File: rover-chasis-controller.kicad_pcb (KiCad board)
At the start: 2 copper layers, 100 x 100 mm, 141 parts, among them J10 GPS Interface, J11 Compass Connection (I2C), J15 External LED (Red), J16 External LED (Yellow), J17 External LED (Green), J22 Ultrasonic Sensor Inputs, J26 Screw_Terminal_01x02, J3 HR911105A_C12074, J36 Motor control, J37 Motor control, J38 Motor control, J39 Motor control, J40 Encoder, J41 Encoder, J42 Encoder, J43 Encoder, J7 TTL, J8 Ultrasonic Sensor Inputs, Q1 MMBT3904_C181119, Q11 MMBT3904_C181119, Q13 MMBT3904_C181119, Q14 MMBT3904_C181119, Q15 SUD50P10-43L-TP, Q17 MMBT3904_C181119, Q22 MMBT3904_C181119, Q23 MMBT3904_C181119, Q24 MMBT3904_C181119, Q25 MMBT3904_C181119, Q26 MMBT3904_C181119, Q27 MMBT3904_C181119, Q28 MMBT3904_C181119, Q29 MMBT3904_C181119, Q30 MMBT3904_C181119, Q31 MMBT3904_C181119, Q32 MMBT3904_C181119, Q33 MMBT3904_C181119, Q34 MMBT3904_C181119, Q35 MMBT3904_C181119, Q6 MMBT3904_C181119, U1 APT2012LVBC/D, U2 APT2012LVBC/D, U3 APT2012LVBC/D, U4 KSZ8081RNAIA-TR, U5 MPU-6050_C24112, U6 AP64500SP-13, U7 APT2012LVBC/D, X1 X1G004451000400

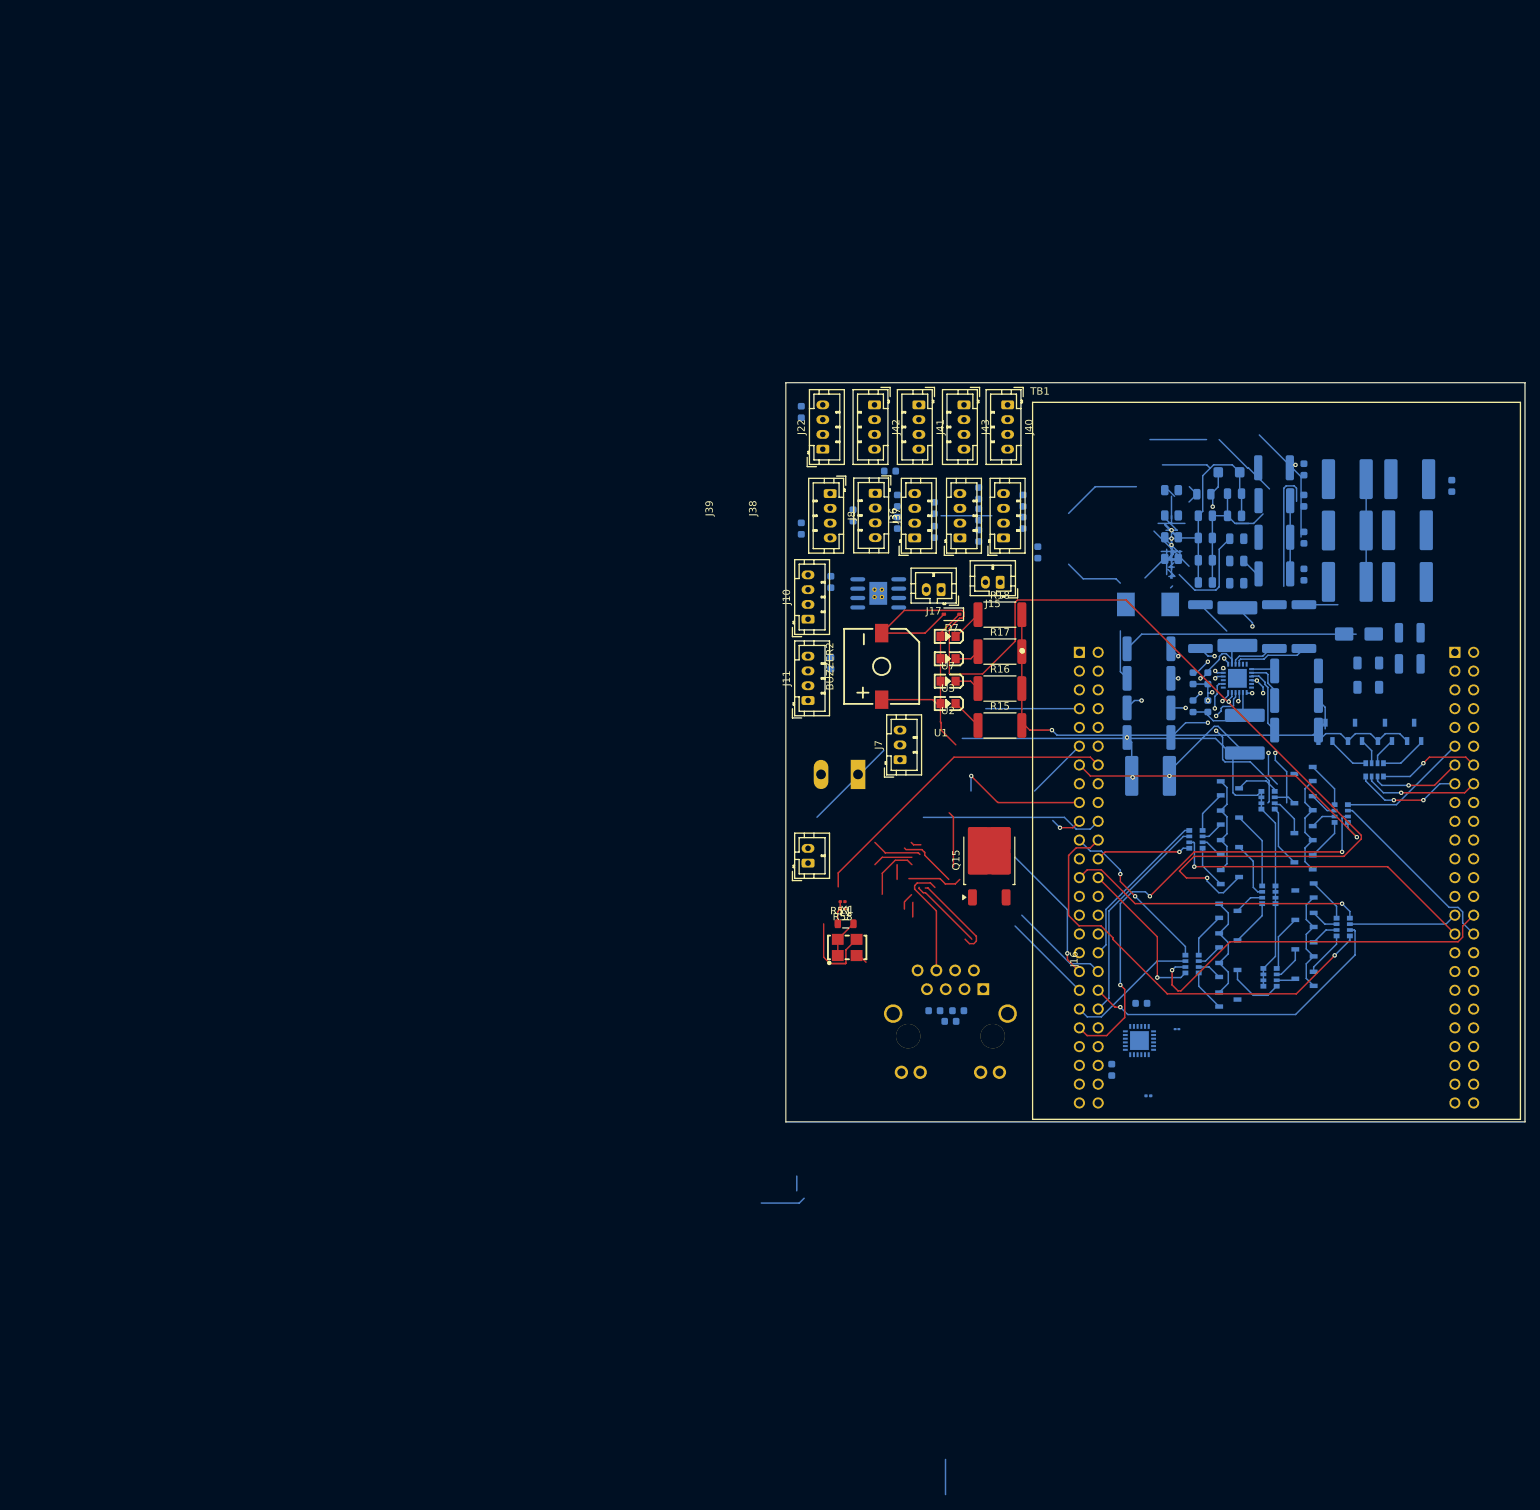
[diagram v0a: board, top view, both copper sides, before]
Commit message: Issue #1: Revised possible PCB design
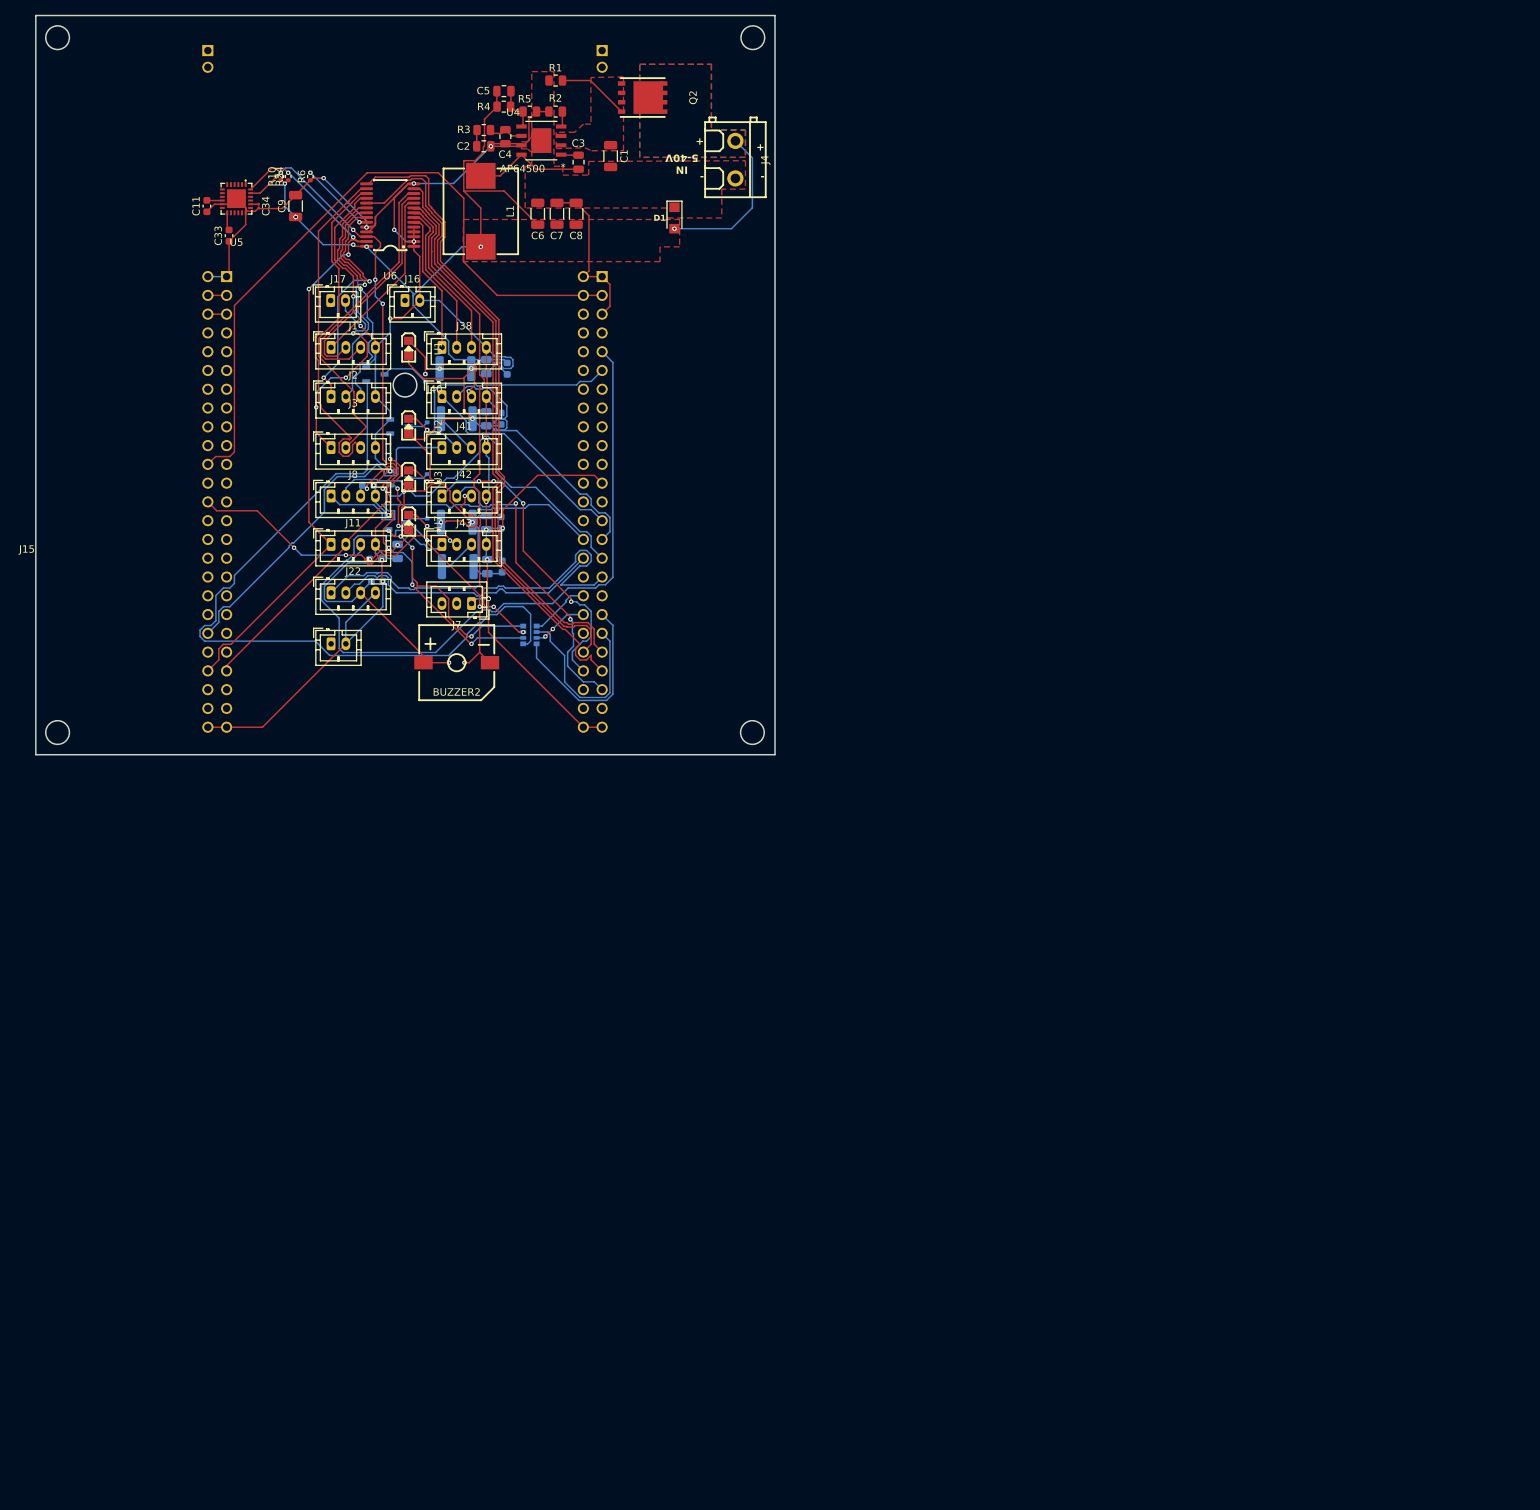
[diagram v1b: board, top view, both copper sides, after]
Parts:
- removed C17, C71, C72, C83, C84, C85, C86, C87, C88, C89, C90, C91, C92, C93, C94: 0.1uF, Capacitor_SMD:C_0603_1608Metric
- removed C18: 10uF, Capacitor_SMD:C_0805_2012Metric
- removed C53: 10uF, Capacitor_SMD:C_2220_5750Metric
- removed C54: 100nF, Capacitor_SMD:C_0805_2012Metric
- removed C55: 2.7nF, Capacitor_SMD:C_0805_2012Metric
- removed C56: 39pF, Capacitor_SMD:C_0805_2012Metric
- removed C57: 47pF, Capacitor_SMD:C_0805_2012Metric
- removed C58, C59, C60: 22 uF, Capacitor_SMD:C_2220_5750Metric
- removed C62: 0.1uF 200V, Capacitor_SMD:C_0603_1608Metric
- removed D10: SMF5V0A, Diode_SMD:D_SMF
- removed D11: SMAJ5.0A, Diode_SMD:D_SMA
- removed FB1: FerriteBead, Inductor_SMD:L_0603_1608Metric
- removed J10: GPS Interface, Connector_JST:JST_PH_B4B-PH-K_1x04_P2.00mm_Vertical
- removed J26: Screw_Terminal_01x02, TerminalBlock:TerminalBlock_Altech_AK300-2_P5.00mm
- removed J36, J37, J39: Motor control, Connector_JST:JST_PH_B4B-PH-K_1x04_P2.00mm_Vertical
- removed L4: 4.7uH, easyeda2kicad:IND-SMD_L7.0-W6.6
- removed Q1, Q11, Q13, Q17, Q22, Q23, Q24, Q25, Q26, Q27, Q28, Q29, Q30, Q31, Q32, Q6: MMBT3904_C181119, easyeda2kicad:SOT-23-3_L2.9-W1.6-P1.90-LS2.8-BR
- removed Q15: SUD50P10-43L-TP, Package_TO_SOT_SMD:TO-252-2
- removed R16, R17, R18: 220, Resistor_SMD:R_2512_6332Metric
- removed R25: 4.3k, Resistor_SMD:R_1210_3225Metric
- removed R57, R58: 330, Resistor_SMD:R_0201_0603Metric
- removed R59, R60, R61, R62, R63, R71, R72, R73, R74: 24, Resistor_SMD:R_2512_6332Metric
- removed R75: 47k, Resistor_SMD:R_0201_0603Metric
- removed R76: 10k, Resistor_SMD:R_1206_3216Metric
- removed R77: 47k T+-1%, Resistor_SMD:R_1206_3216Metric
- removed R78: 200k, Resistor_SMD:R_0805_2012Metric
- removed R79: 16k, Resistor_SMD:R_0805_2012Metric
- removed R80: 120k, Resistor_SMD:R_0805_2012Metric
- removed R81: 22.1k, Resistor_SMD:R_0805_2012Metric
- removed RN10, RN11, RN12: 4D03WGJ0102T5E (10k), easyeda2kicad:RES-ARRAY-SMD_0603-8P-L3.2-W1.6-BL
- removed RN2, RN3, RN4, RN5: 4D03WGJ0102T5E (1k), easyeda2kicad:RES-ARRAY-SMD_0603-8P-L3.2-W1.6-BL
- removed X1: X1G004451000400, easyeda2kicad:OSC-SMD_4P-L5.0-W3.2-BL_SG5032
- added D1: SMF5V0A, Diode_SMD:D_SMF, F.Cu at (86.5, 27.4)
- added J1: Motor control, Connector_JST:JST_PH_B4B-PH-K_1x04_P2.00mm_Vertical, F.Cu at (40.0, 44.9)
- added J2: Motor control, Connector_JST:JST_PH_B4B-PH-K_1x04_P2.00mm_Vertical, F.Cu at (40.0, 51.5)
- added J4: Screw_Terminal_01x02, easyeda2kicad:CONN-TH_2P-P5.08, F.Cu at (94.7, 19.5)
- added Q2: HSBA100P04_C2987717, easyeda2kicad:DFN-8_L5.7-W5.1-P1.27-LS6.1-BL-1, F.Cu at (82.2, 11.1)
- added R10: 4.3k, Resistor_SMD:R_0402_1005Metric, F.Cu at (33.2, 21.8)
- added R2: 200k, Resistor_SMD:R_0805_2012Metric, F.Cu at (70.4, 13.0)
- added R3: 16k, Resistor_SMD:R_0805_2012Metric, F.Cu at (60.7, 15.5)
- added R4: 120k, Resistor_SMD:R_0805_2012Metric, F.Cu at (63.4, 12.3)
- added R5: 22.1k, Resistor_SMD:R_0805_2012Metric, F.Cu at (66.9, 13.0)
- added R6: 10k, Resistor_SMD:R_0402_1005Metric, F.Cu at (37.2, 21.8)
- added R7: 220, Resistor_SMD:R_0402_1005Metric, B.Cu at (53.0, 55.5)
- added R8: 220, Resistor_SMD:R_0402_1005Metric, B.Cu at (53.0, 62.5)
- added R9: 220, Resistor_SMD:R_0402_1005Metric, B.Cu at (53.0, 68.6)
- C1: value 0.1uF -> 10uF; footprint Capacitor_SMD:C_0603_1608Metric -> Capacitor_SMD:C_1206_3216Metric; moved to F.Cu
- C11, C33, C34, U5: moved to F.Cu
- C2: value 22uF -> 2.7nF; footprint Capacitor_SMD:C_2220_5750Metric -> Capacitor_SMD:C_0805_2012Metric; moved to F.Cu
- C3: value 2.2uF -> 100nF; footprint Capacitor_SMD:C_2220_5750Metric -> Capacitor_SMD:C_0805_2012Metric; moved to F.Cu
- C4: value 0.1uF -> 39pF; footprint Capacitor_SMD:C_0603_1608Metric -> Capacitor_SMD:C_0805_2012Metric; moved to F.Cu
- C5: value 22pF -> 47pF; footprint Capacitor_SMD:C_2220_5750Metric -> Capacitor_SMD:C_0805_2012Metric; moved to F.Cu
- C6, C8: value 0.1uF -> 22 uF; footprint Capacitor_SMD:C_0603_1608Metric -> Capacitor_SMD:C_1206_3216Metric; moved to F.Cu
- C7: value 22uF -> 22 uF; footprint Capacitor_SMD:C_2220_5750Metric -> Capacitor_SMD:C_1206_3216Metric; moved to F.Cu
- C9: value 22uF -> 10uF; footprint Capacitor_SMD:C_2220_5750Metric -> Capacitor_SMD:C_1206_3216Metric; moved to F.Cu
- D7: moved to B.Cu
- J3: value HR911105A_C12074 -> Motor control; footprint easyeda2kicad:RJ45-TH_HR911105A -> Connector_JST:JST_PH_B4B-PH-K_1x04_P2.00mm_Vertical; moved to F.Cu
- L1: value BLM21PG331SN1D -> 3.3uH; footprint Inductor_SMD:L_0805_2012Metric -> easyeda2kicad:IND-SMD_L11.6-W10.1
- R1: value 24 -> 47k; footprint Resistor_SMD:R_2512_6332Metric -> Resistor_SMD:R_0805_2012Metric; moved to F.Cu
- R15: footprint Resistor_SMD:R_2512_6332Metric -> Resistor_SMD:R_0402_1005Metric; moved to B.Cu
- R24: footprint Resistor_SMD:R_1210_3225Metric -> Resistor_SMD:R_0402_1005Metric; moved to F.Cu
- TB1: footprint STM32F4DISCOVERY:MODULE_STM32F4DISCOVERY -> stm32:MODULE_STM32F4DISCOVERY; moved to B.Cu
- U4: value KSZ8081RNAIA-TR -> AP64500; footprint easyeda2kicad:QFN-24_L4.0-W4.0-P0.50-BL-EP2.6 -> easyeda2kicad:AP64500SP-13; moved to F.Cu
- U6: value AP64500SP-13 -> PCA9685PW,118; footprint easyeda2kicad:SOIC-8_L4.9-W3.9-P1.27-LS6.0-BL-EP-1 -> easyeda2kicad:TSSOP-28_L9.7-W4.4-P0.65-LS6.4-TL; moved to F.Cu
- moved C11 169.2 mm to (23.2, 25.8)
- moved U5 167.0 mm to (27.2, 24.8)
- moved C34 166.8 mm to (30.2, 25.8), turned to -90 degrees
- moved R24 163.8 mm to (34.2, 21.8), turned to 90 degrees
- moved C33 161.3 mm to (26.2, 29.8), turned to 90 degrees
- moved Q35 140.4 mm to (49.0, 68.5), turned to 180 degrees
- moved C9 139.5 mm to (35.2, 25.8)
- moved Q34 137.7 mm to (49.2, 62.6), turned to 180 degrees
- moved Q14 137.3 mm to (46.0, 48.5), turned to 180 degrees
- moved Q33 135.7 mm to (49.2, 55.6), turned to 180 degrees
- moved C2 130.1 mm to (60.7, 17.7), turned to 0 degrees
- moved C6 129.0 mm to (68.0, 26.8), turned to 90 degrees
- moved TB1 128.4 mm to (50.0, 50.0), turned to 180 degrees
- moved C5 127.4 mm to (63.4, 10.2), turned to 0 degrees
- moved C3 125.7 mm to (73.5, 19.8), turned to -90 degrees
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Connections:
- BUZZER2 pad 2: /Buzzer_Collector -> /BUZZER_OUT
- C1 pad 1: GND -> unconnected-(C1-Pad1)
- C1 pad 2: Net-(U4-VDD_1.2) -> GND
- C2 pad 1: Net-(U4-VDDA_3.3) -> Net-(C2-Pad1)
- C3 pad 1: Net-(U4-VDD_1.2) -> Net-(U4-BST)
- C3 pad 2: GND -> Net-(U4-SW)
- C4 pad 1: GND -> Net-(U4-COMP)
- C4 pad 2: Net-(U4-VDDA_3.3) -> GND
- C5 pad 1: GND -> VCC (5V)
- C5 pad 2: Net-(X1-OUT) -> Net-(U4-FB)
- C6 pad 1: GND -> VCC (5V)
- C6 pad 2: Net-(X1-OE/~{ST}) -> GND
- C7 pad 1: Net-(X1-OE/~{ST}) -> VCC (5V)
- C8 pad 1: GND -> VCC (5V)
- C8 pad 2: VCC (3.3V) -> GND
- C9 pad 1: VCC (3.3V) -> VCC (5V)
- D7 pad 2: /Buzzer_Collector -> /BUZZER_OUT
- J11 pad 1: /COMPASS_SDA -> /SDA
- J11 pad 2: /COMPASS_SCL -> /SCL
- J3 pad 1: /TXP -> /MOTOR4_PWM
- J3 pad 2: /TXM -> /MOTOR4_FWD
- J3 pad 3: /RXP -> /MOTOR4_RVR
- J3 pad 4: Net-(C72-Pad1) -> GND
- J38 pad 1: /Motor_PWM_Collector_4 -> /MOTOR1_PWM
- J38 pad 2: /Motor_F_Collector_4 -> /MOTOR1_FWD
- J38 pad 3: /Motor_R_Collector_4 -> /MOTOR1_RVR
- J7 pad 1: /TTL_RX -> GND
- J7 pad 3: GND -> /TTL_RX
- L1 pad 1: VCC (3.3V) -> Net-(U4-SW)
- L1 pad 2: Net-(X1-OE/~{ST}) -> VCC (5V)
- R1 pad 1: Net-(U4-XI) -> Net-(Q2-G)
- R1 pad 2: Net-(X1-OUT) -> GND
- R24 pad 1: VCC (3V) -> VCC (5V)
- R24 pad 2: /COMPASS_SDA -> /SDA
- TB1 pad P1_11: /ETH_REF_CLK -> /ENC2_B
- TB1 pad P1_12: /TTL_TX -> unconnected-(TB1-PA0-WKUP-PadP1_12)
- TB1 pad P1_13: /MOTOR2_PWM -> unconnected-(TB1-PA3-PadP1_13)
- TB1 pad P1_14: /ETH_MDIO -> unconnected-(TB1-PA2-PadP1_14)
- TB1 pad P1_15: /ENC2_A -> unconnected-(TB1-PA5-PadP1_15)
- TB1 pad P1_16: /POWER_SUPPLY_ADC -> unconnected-(TB1-PA4-PadP1_16)
- TB1 pad P1_17: /ETH_CRS_DV -> unconnected-(TB1-PA7-PadP1_17)
- TB1 pad P1_18: /ENC3_A -> unconnected-(TB1-PA6-PadP1_18)
- TB1 pad P1_19: /ETH_RXD1 -> unconnected-(TB1-PC5-PadP1_19)
- TB1 pad P1_20: /ETH_RXD0 -> unconnected-(TB1-PC4-PadP1_20)
- TB1 pad P1_21: /MOTOR4_PWM -> unconnected-(TB1-PB1-PadP1_21)
- TB1 pad P1_22: /MOTOR3_PWM -> unconnected-(TB1-PB0-PadP1_22)
- TB1 pad P1_24: /BUZZER_OUT -> unconnected-(TB1-PB2-PadP1_24)
- TB1 pad P1_25: /LED_YELLOW -> unconnected-(TB1-PE7-PadP1_25)
- TB1 pad P1_26: /LED_GREEN -> unconnected-(TB1-PE8-PadP1_26)
- TB1 pad P1_30: unconnected-(TB1-PE12-PadP1_30) -> /US_SENSOR1_TRIG
- TB1 pad P1_33: unconnected-(TB1-PE15-PadP1_33) -> /US_SENSOR2_TRIG
- TB1 pad P1_34: /MOTOR1_PWM -> unconnected-(TB1-PB10-PadP1_34)
- TB1 pad P1_35: /ETH_TX_EN -> unconnected-(TB1-PB11-PadP1_35)
- TB1 pad P1_36: /ETH_TXD0 -> /LED_BLUE_4
- TB1 pad P1_37: /ETH_TXD1 -> /LED_BLUE_1
- TB1 pad P1_38: /MOTOR3_FWD -> /LED_BLUE_2
- TB1 pad P1_39: /MOTOR4_FWD -> /LED_BLUE_3
- TB1 pad P1_40: /MOTOR1_FWD -> unconnected-(TB1-PD8-PadP1_40)
- TB1 pad P1_41: /MOTOR2_FWD -> /LED_GREEN
- TB1 pad P1_42: /US_SENSOR1_TRIG -> /LED_YELLOW
- TB1 pad P1_43: /US_SENSOR2_TRIG -> /LED_RED
- TB1 pad P1_7: /ETH_MDC -> /POWER_SUPPLY_ADC
- TB1 pad P1_9: unconnected-(TB1-PC3-PadP1_9) -> /ENC3_A
- TB1 pad P2_11: /LED_RED -> unconnected-(TB1-PE6-PadP2_11)
- TB1 pad P2_13: /LED_BLUE_3 -> unconnected-(TB1-PE4-PadP2_13)
- TB1 pad P2_14: /LED_BLUE_4 -> unconnected-(TB1-PE5-PadP2_14)
- TB1 pad P2_15: /LED_BLUE_1 -> unconnected-(TB1-PE2-PadP2_15)
- TB1 pad P2_16: /LED_BLUE_2 -> unconnected-(TB1-PE3-PadP2_16)
- TB1 pad P2_23: /COMPASS_SCL -> unconnected-(TB1-PB6-PadP2_23)
- TB1 pad P2_24: /COMPASS_SDA -> unconnected-(TB1-PB7-PadP2_24)
- TB1 pad P2_26: unconnected-(TB1-PB5-PadP2_26) -> /ENC3_B
- TB1 pad P2_28: /ENC2_B -> unconnected-(TB1-PB3-PadP2_28)
- TB1 pad P2_29: /MOTOR3_RVR -> unconnected-(TB1-PD5-PadP2_29)
- TB1 pad P2_30: /MOTOR4_RVR -> unconnected-(TB1-PD6-PadP2_30)
- TB1 pad P2_31: /MOTOR1_RVR -> unconnected-(TB1-PD3-PadP2_31)
- TB1 pad P2_32: /MOTOR2_RVR -> unconnected-(TB1-PD4-PadP2_32)
- TB1 pad P2_34: /GPS_RX -> unconnected-(TB1-PD2-PadP2_34)
- TB1 pad P2_35: /GPS_TX -> unconnected-(TB1-PC12-PadP2_35)
- TB1 pad P2_38: /TTL_RX -> unconnected-(TB1-PC11-PadP2_38)
- TB1 pad P2_40: unconnected-(TB1-PA15-PadP2_40) -> /ENC2_A
- TB1 pad P2_43: /MPU_SCL -> /SCL
- TB1 pad P2_44: unconnected-(TB1-PA9-PadP2_44) -> /SDA
- TB1 pad P2_46: /MPU_SDA -> unconnected-(TB1-PC9-PadP2_46)
- TB1 pad P2_48: /ENC3_B -> unconnected-(TB1-PC7-PadP2_48)
- U4 pad 1: Net-(U4-VDD_1.2) -> Net-(U4-BST)
- U4 pad 2: Net-(U4-VDDA_3.3) -> unconnected-(C1-Pad1)
- U4 pad 3: /RXM -> unconnected-(C1-Pad1)
- U4 pad 4: /RXP -> Net-(U4-RT/CLK)
- U4 pad 5: /TXM -> Net-(U4-FB)
- U4 pad 6: /TXP -> Net-(U4-COMP)
- U4 pad 7: unconnected-(U4-XO-Pad7) -> GND
- U4 pad 8: Net-(U4-XI) -> Net-(U4-SW)
- U5 pad 23: /MPU_SCL -> /SCL
- U5 pad 24: /MPU_SDA -> /SDA
- U6 pad 1: Net-(U6-BST) -> GND
- U6 pad 2: Net-(Q15-S) -> GND
- U6 pad 3: Net-(Q15-S) -> GND
- U6 pad 4: Net-(U6-RT/CLK) -> GND
- U6 pad 5: Net-(U6-FB) -> GND
- U6 pad 6: Net-(U6-COMP) -> /MOTOR1_PWM
- U6 pad 7: GND -> /MOTOR1_FWD
- U6 pad 8: Net-(U6-SW) -> /MOTOR1_RVR
- U6 pad 9: GND -> /BUZZER_OUT
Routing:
- net GND: track 174.1 -> 349.1 mm, vias 6 -> 21
- net /Buzzer_Collector: track 144.8 -> 0.00 mm, vias 1 -> 0
- net /ENC3_A: track 0.00 -> 104.5 mm
- net /transistor_array4/B1: track 5.64 -> 101.1 mm
- net Net-(TB1-VDD-PadP1_3): track 0.00 -> 93.2 mm
- net /SDA: track 0.00 -> 93.0 mm, vias 0 -> 4
- net /SCL: track 0.00 -> 92.8 mm, vias 0 -> 4
- net VCC (5V): track 169.9 -> 252.6 mm, vias 1 -> 18
- net /LED_GREEN: track 20.9 -> 86.0 mm, vias 1 -> 0
- net /LED_RED: track 17.7 -> 79.9 mm
- net /BUZZER_OUT: track 12.9 -> 71.2 mm
- net /US_SENSOR2_TRIG: track 0.00 -> 53.5 mm
- net /US_SENSOR1_ECHO: track 0.00 -> 51.3 mm
- net /LED_Collector_1: track 57.3 -> 6.55 mm, vias 1 -> 0
- net /ENC2_A: track 0.00 -> 48.6 mm
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- added copper zone on F.Cu, net GND
- added copper zone on B.Cu, net VCC (5V)
- added copper zone on F.Cu, net VCC (5V)
- added copper zone on F.Cu, net unconnected-(C1-Pad1)
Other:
- outline, holes or cut-outs redrawn
- board text added: "+"
- board text added: "-"
- board text added: "IN 5-40V"

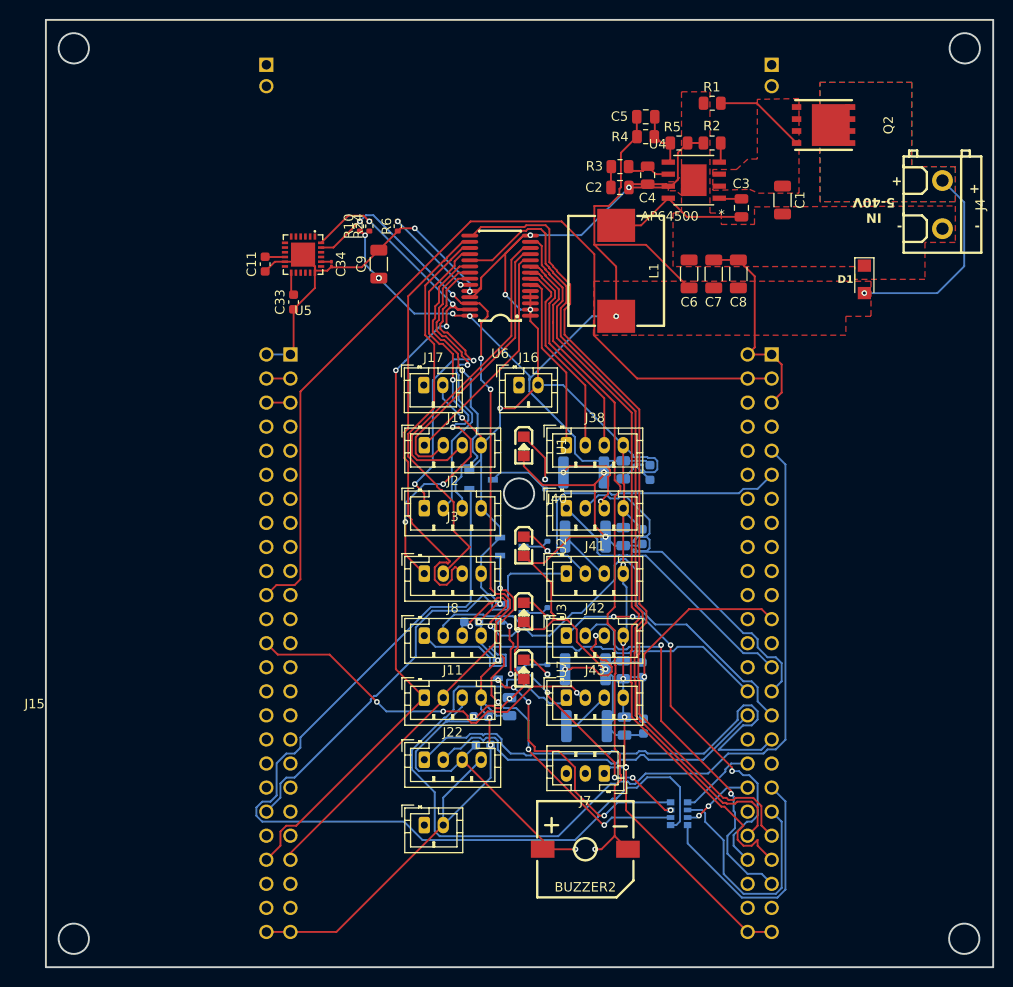
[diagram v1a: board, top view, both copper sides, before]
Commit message: Issue #1: Updated PCB layout — mounting holes, silk screen, and DRC fixes
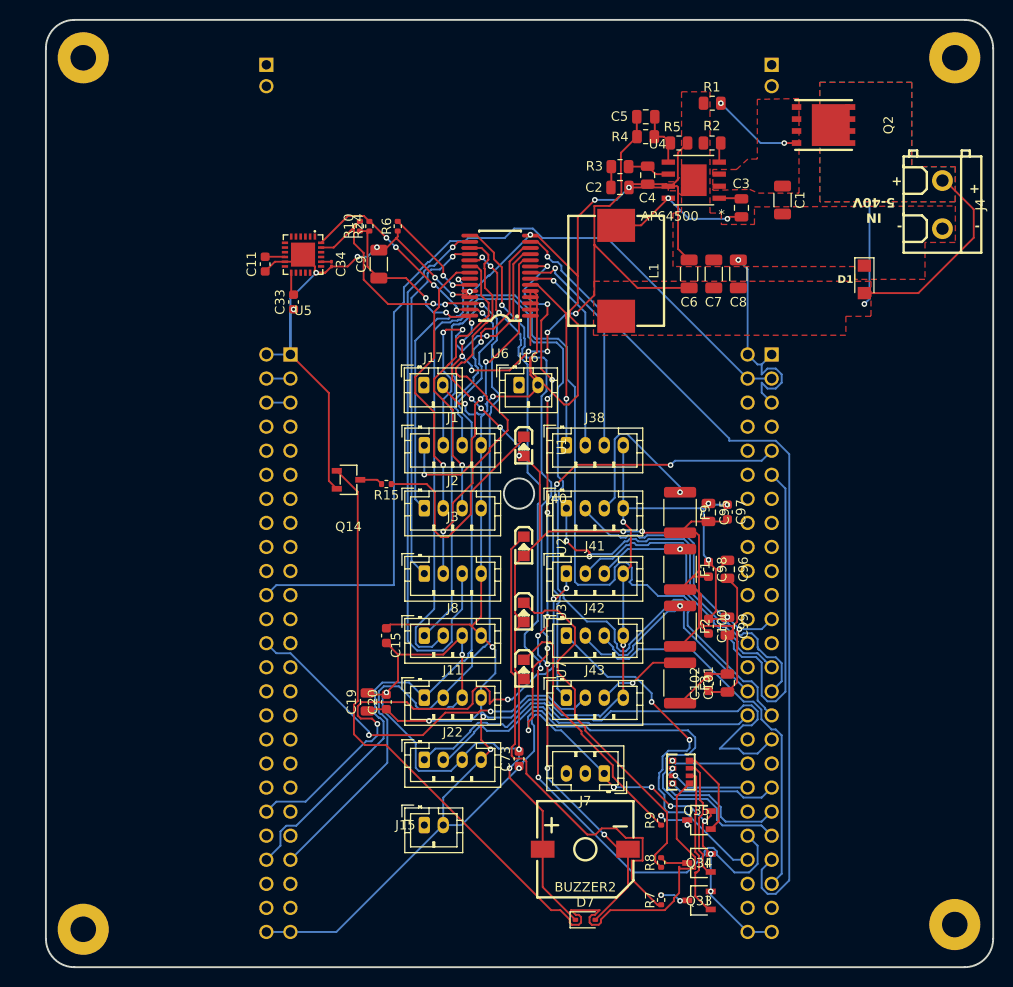
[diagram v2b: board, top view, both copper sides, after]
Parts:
- added MK1: M2.5, MountingHole:MountingHole_2.7mm_M2.5_Pad, F.Cu at (96.0, 4.00)
- added MK1: M2.5, MountingHole:MountingHole_2.7mm_M2.5_Pad, F.Cu at (4.00, 4.00)
- added MK1: M2.5, MountingHole:MountingHole_2.7mm_M2.5_Pad, F.Cu at (96.0, 95.5)
- added MK1: M2.5, MountingHole:MountingHole_2.7mm_M2.5_Pad, F.Cu at (4.00, 96.0)
- C100, C101, C102, C15, C19, C20, C73, C95, C96, C97, C98, C99, D7, F1, F2, F3, F9, Q14, Q33, Q34, Q35, R15, R7, R8, R9, RN1: moved to F.Cu
- moved Q33 42.3 mm to (69.0, 93.0), turned to 0 degrees
- moved R7 39.2 mm to (65.0, 92.9)
- moved Q34 33.0 mm to (69.0, 89.0), turned to 0 degrees
- moved R8 29.0 mm to (65.0, 89.0)
- moved Q35 25.6 mm to (69.0, 84.5), turned to 0 degrees
- moved C102 23.1 mm to (70.0, 70.0)
- moved R9 19.9 mm to (65.0, 84.5)
- moved C97 18.9 mm to (72.0, 52.0), turned to -90 degrees
- moved R15 16.8 mm to (36.0, 49.0), turned to 180 degrees
- moved C99 15.1 mm to (72.0, 64.0)
- moved C19 15.0 mm to (34.0, 72.0)
- moved Q14 14.0 mm to (32.0, 48.5)
- moved C100 12.6 mm to (70.0, 64.0)
- moved C96 11.5 mm to (72.0, 58.0)
- moved C101 11.1 mm to (72.0, 70.0)
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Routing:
- net GND: track 349.1 -> 436.4 mm, vias 21 -> 32
- net /US_SENSOR1_TRIG: track 43.7 -> 109.5 mm
- net /US_SENSOR1_ECHO: track 51.3 -> 115.5 mm
- net /ENC3_A: track 104.5 -> 47.7 mm, vias 0 -> 2
- net Net-(U2-K): track 3.13 -> 52.4 mm, vias 1 -> 0
- net Net-(U3-K): track 3.13 -> 38.3 mm, vias 1 -> 0
- net VCC (5V): track 252.6 -> 286.2 mm, vias 18 -> 20
- net /transistor_array4/B2: track 43.8 -> 16.0 mm, vias 4 -> 0
- net /ENC2_B: track 33.5 -> 59.1 mm
- net Net-(U7-K): track 3.13 -> 27.7 mm, vias 1 -> 0
- net /transistor_array4/B4: track 28.9 -> 9.19 mm, vias 4 -> 0
- net Net-(U1-K): track 5.45 -> 24.6 mm, vias 1 -> 0
- net /transistor_array4/B3: track 30.5 -> 12.7 mm, vias 6 -> 0
- net /LED_GREEN: track 86.0 -> 102.2 mm, vias 0 -> 3
- net /LED_BLUE_1: track 26.3 -> 11.5 mm, vias 0 -> 1
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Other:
- outline, holes or cut-outs redrawn
